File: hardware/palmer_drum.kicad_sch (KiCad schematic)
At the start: 8 parts, among them J1 EURO_PWR, J2 SERGE_PWR

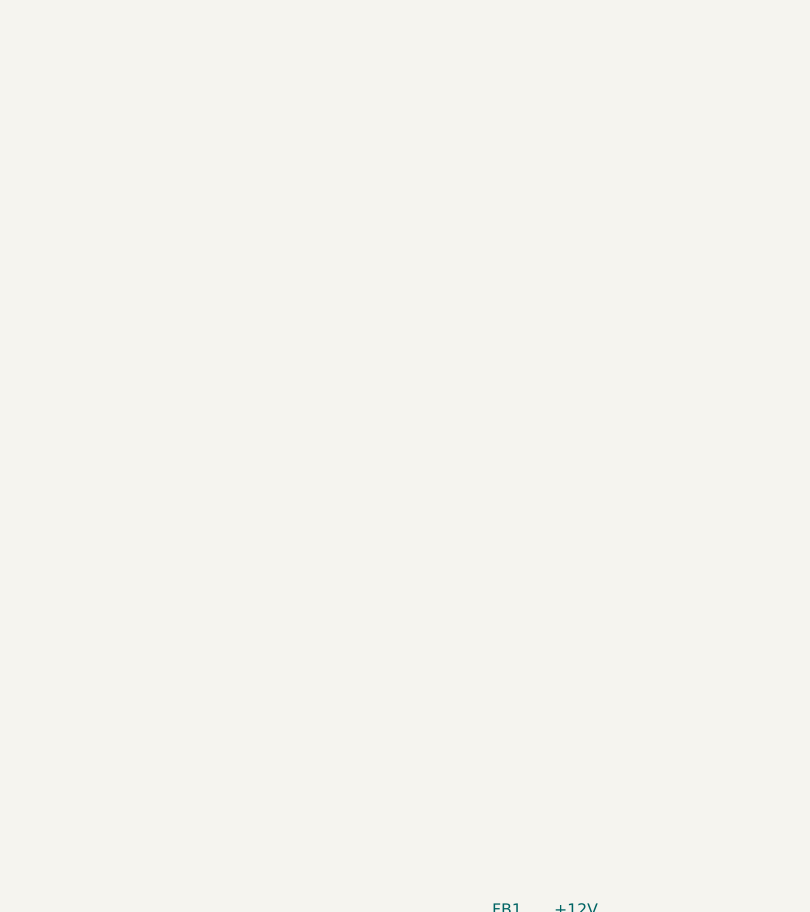
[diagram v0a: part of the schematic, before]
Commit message: Added ki-Lime-pi-pico library version 2.1.3
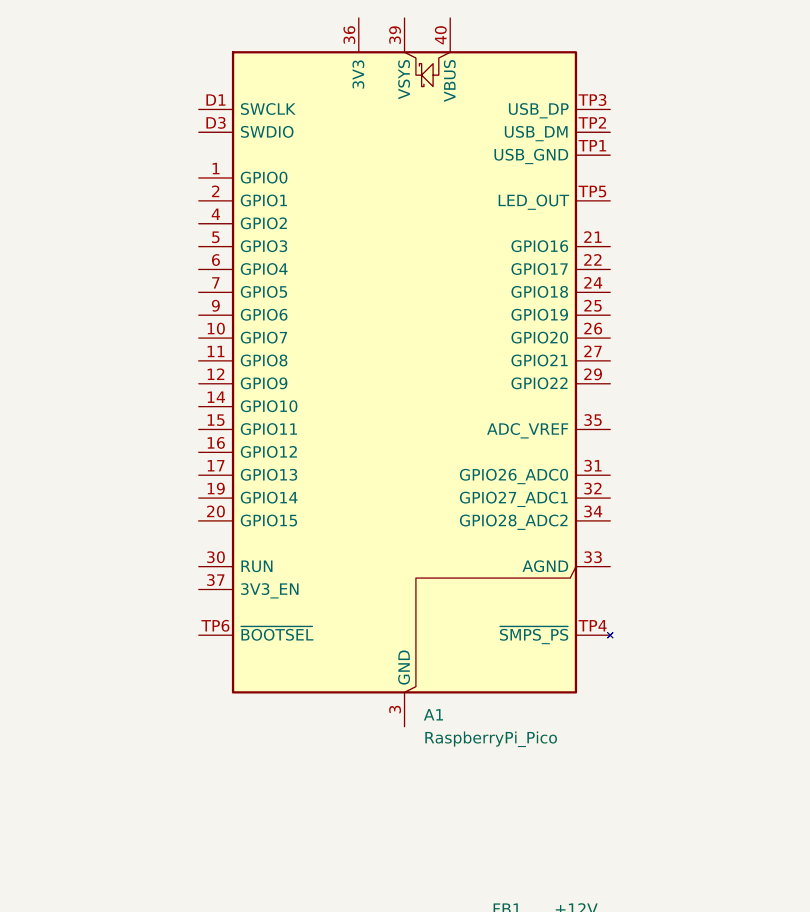
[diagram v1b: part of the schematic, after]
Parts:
- added A1: RaspberryPi_Pico, Module_RaspberryPi_Pico:RaspberryPi_Pico_Original_SMD, symbol MCU_Module_RaspberryPi_Pico:RaspberryPi_Pico_SecondaryPins
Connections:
- new net: A1.13 (GND), A1.18 (GND), A1.23 (GND), A1.28 (GND), A1.3 (GND), A1.38 (GND), A1.8 (GND), A1.D2 (GND)
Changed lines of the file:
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@@
+	)
+	(symbol
+		(lib_id "MCU_Module_RaspberryPi_Pico:RaspberryPi_Pico_SecondaryPins")
+		(at 64.77 81.28 0)
+		(unit 1)
+		(body_style 1)
+		(exclude_from_sim no)
+		(in_bom yes)
+		(on_board yes)
+		(in_pos_files yes)
+		(dnp no)
+		(fields_autoplaced yes)
+		(property "Reference" "A1"
+			(at 66.9133 118.11 0)
+			(show_name no)
+			(do_not_autoplace no)
+			(effects
+				(font
+					(size 1.27 1.27)
+				)
+				(justify left)
+			)
+		)
+		(property "Value" "RaspberryPi_Pico"
+			(at 66.9133 120.65 0)
+			(show_name no)
+			(do_not_autoplace no)
+			(effects
+				(font
+					(size 1.27 1.27)
+				)
+				(justify left)
+			)
+		)
+		(property "Footprint" "Module_RaspberryPi_Pico:RaspberryPi_Pico_Original_SMD"
+			(at 64.77 130.81 0)
+			(hide yes)
+			(show_name no)
+			(do_not_autoplace no)
+			(effects
+				(font
+					(size 1.27 1.27)
+				)
+			)
+		)
+		(property "Datasheet" "https://datasheets.raspberrypi.com/pico/pico-datasheet.pdf"
+			(at 64.77 133.35 0)
+			(hide yes)
+			(show_name no)
+			(do_not_autoplace no)
+			(effects
+				(font
+					(size 1.27 1.27)
+				)
+			)
+		)
+		(property "Description" "Versatile and inexpensive microcontroller module (with full pinout for test point and debug connections) powered by RP2040 dual-core Arm Cortex-M0+ processor up to 133 MHz, 264kB SRAM, 2MB QSPI flash"
+			(at 64.77 135.89 0)
+			(hide yes)
+			(show_name no)
+			(do_not_autoplace no)
+			(effects
+				(font
+					(size 1.27 1.27)
+				)
+			)
+		)
+		(pin "1"
+		)
+		(pin "13"
+		)
+		(pin "16"
+		)
+		(pin "26"
+		)
+		(pin "28"
+		)
+		(pin "22"
+		)
+		(pin "19"
+		)
+		(pin "2"
+		)
+		(pin "15"
+		)
+		(pin "9"
+		)
+		(pin "25"
+		)
+		(pin "23"
+		)
+		(pin "7"
+		)
+		(pin "5"
+		)
+		(pin "6"
+		)
+		(pin "12"
+		)
+		(pin "10"
+		)
+		(pin "24"
+		)
+		(pin "4"
+		)
+		(pin "27"
+		)
+		(pin "14"
+		)
+		(pin "8"
+		)
+		(pin "11"
+		)
+		(pin "21"
+		)
+		(pin "20"
+		)
+		(pin "3"
+		)
+		(pin "17"
+		)
+		(pin "18"
+		)
+		(pin "36"
+		)
+		(pin "D1"
+		)
+		(pin "38"
+		)
+		(pin "29"
+		)
+		(pin "37"
+		)
+		(pin "TP1"
+		)
+		(pin "32"
+		)
+		(pin "TP6"
+		)
+		(pin "TP2"
+		)
+		(pin "TP4"
+		)
+		(pin "TP5"
+		)
+		(pin "D3"
+		)
+		(pin "33"
+		)
+		(pin "30"
+		)
+		(pin "40"
+		)
+		(pin "31"
+		)
+		(pin "D2"
+		)
+		(pin "34"
+		)
+		(pin "35"
+		)
+		(pin "39"
+		)
+		(pin "TP3"
+		)
+		(instances
+			(project "palmer_drum"
+				(path "/a1c8c82f-599d-4a64-8030-47d97f65a492"
+					(reference "A1")
+					(unit 1)
+				)
+			)
+		)
 	)
 	(symbol

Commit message: Added a hierichal sheet for the RP2040
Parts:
- removed A1: RaspberryPi_Pico, Module_RaspberryPi_Pico:RaspberryPi_Pico_Original_SMD, symbol MCU_Module_RaspberryPi_Pico:RaspberryPi_Pico_SecondaryPins
- added C4: 100nF, symbol Device:C
- added C5: 220nF, symbol Device:C
- added U3: L7805, Package_QFP:Hitachi_FP80B_PQFP-80_14x20mm_P0.8mm, symbol Regulator_Linear:L7805
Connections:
- net +12V: now also D1.1 (K), C5.1, U3.1 (IN); no longer FB1.2
- net -12V: now also D2.2 (A); no longer FB2.2
- net GND: now also C4.2, C5.2, U3.2 (GND)
- net at FB1.1: now also J1.1 (Pin_1), J1.2 (Pin_2), J2.1 (Pin_1); no longer D1.1 (K)
- net at J1.10 (Pin_10), J1.9 (Pin_9), J2.4 (Pin_4): now also FB2.1; no longer D2.1 (K)
- new net: D1.2 (A), FB1.2
- new net: D2.1 (K), FB2.2
- new net +5V: C4.1, U3.3 (OUT)
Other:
- added sheet MCU (mcu.kicad_sch)
- moved on the sheet: D1, D2, FB1, FB2

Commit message: Schematic update
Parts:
- added C6, C7: 10uF, symbol Device:C_Polarized
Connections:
- net +12V: now also C6.1
- net -12V: now also C7.2
- net GND: now also C6.2, C7.1
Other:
- moved on the sheet: C1, C2, C4, C5, U3

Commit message: Updated schematic
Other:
- added sheet INPUT_OUTPUT (input_output.kicad_sch)
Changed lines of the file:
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@@
+	)
+	(sheet
+		(at 71.12 53.975)
+		(size 34.925 39.37)
+		(exclude_from_sim no)
+		(in_bom yes)
+		(on_board yes)
+		(dnp no)
+		(fields_autoplaced yes)
+		(stroke
+			(width 0.1524)
+			(type solid)
+		)
+		(fill
+			(color 0 0 0 0)
+		)
+		(property "Sheetname" "INPUT_OUTPUT"
+			(at 71.12 53.2634 0)
+			(show_name no)
+			(do_not_autoplace no)
+			(effects
+				(font
+					(size 1.27 1.27)
+				)
+				(justify left bottom)
+			)
+		)
+		(property "Sheetfile" "input_output.kicad_sch"
+			(at 71.12 93.9296 0)
+			(show_name no)
+			(do_not_autoplace no)
+			(effects
+				(font
+					(size 1.27 1.27)
+				)
+				(justify left top)
+			)
+		)
+		(instances
+			(project "palmer_drum"
+				(path "/a1c8c82f-599d-4a64-8030-47d97f65a492"
+					(page "5")
+				)
+			)
+		)
 	)
 	(sheet
